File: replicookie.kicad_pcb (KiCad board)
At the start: 2 copper layers, 152.4 x 114.3 mm, 130 parts, among them J1001 Conn_02x03_Odd_Even, J1002 Conn_01x08_Female, J1003 Screw_Terminal_01x04, J1005 Conn_01x08_Female, J1101 Conn_02x03_Odd_Even, J1102 Conn_01x08_Female, J1103 Screw_Terminal_01x04, J1105 Conn_01x08_Female, J1201 Conn_02x03_Odd_Even, J1202 Conn_01x08_Female, J1203 Screw_Terminal_01x04, J1205 Conn_01x08_Female, J1301 Conn_02x03_Odd_Even, J1302 Conn_01x08_Female, J1303 Screw_Terminal_01x04, J1305 Conn_01x08_Female, J1401 Conn_02x03_Odd_Even, J1402 Conn_01x08_Female, J1403 Screw_Terminal_01x04, J1405 Conn_01x08_Female, J301 JK0654219, J401 USB_A, J402 USB_A, J701 Conn_02x03_Odd_Even, J702 Conn_01x08_Female, J703 Screw_Terminal_01x04, J705 Conn_01x08_Female, J801 Conn_02x03_Odd_Even, J802 Conn_01x08_Female, J803 Screw_Terminal_01x04, J805 Conn_01x08_Female, J901 Conn_02x03_Odd_Even, J902 Conn_01x08_Female, J903 Screw_Terminal_01x04, J905 Conn_01x08_Female, P2 TFM-115-01-F-D-A, P3 TFM-120-01-F-D-A, U201 DS1307ZN+, U301 MIC33050-4YHL, U302 KSZ9031RNXCA, U303 ASDMB-25.000MHz, U304 74LVC2G07, U305 TXS0102DCU, U401 ASDMB-24.000MHz-C, U402 ASDMB-26.000MHz-C, U403 USB3343, U404 74LVC1G07, U405 USB2514B_Bi, X201 ASE-xxxMHz

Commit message: Place motor drivers, start layout of Ethernet PHY
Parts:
- removed the C327 at (118.7, 9.74)
- added C312: 0.1U, Capacitor_SMD:C_0402_1005Metric, F.Cu at (156.8, 45.1)
- C201, C315, C401, C402, C403, C404, C405, C406, C408, C409: footprint Capacitor_SMD:C_0603_1608Metric -> Capacitor_SMD:C_0402_1005Metric
- C301: footprint Capacitor_SMD:C_0603_1608Metric -> Capacitor_SMD:C_0402_1005Metric; moved to B.Cu
- C302: renamed from C329; footprint Capacitor_SMD:C_0603_1608Metric -> Capacitor_SMD:C_0402_1005Metric
- C303: renamed from C302; footprint Capacitor_SMD:C_0603_1608Metric -> Capacitor_SMD:C_0402_1005Metric; moved to B.Cu
- C304: renamed from C330; footprint Capacitor_SMD:C_0603_1608Metric -> Capacitor_SMD:C_0402_1005Metric
- C310: renamed from C306; footprint Capacitor_SMD:C_0603_1608Metric -> Capacitor_SMD:C_0402_1005Metric
- C311: renamed from C309; footprint Capacitor_SMD:C_0603_1608Metric -> Capacitor_SMD:C_0402_1005Metric
- C313: renamed from C310; footprint Capacitor_SMD:C_0603_1608Metric -> Capacitor_SMD:C_0402_1005Metric
- C314: renamed from C311; footprint Capacitor_SMD:C_0603_1608Metric -> Capacitor_SMD:C_0402_1005Metric
- C316: renamed from C312; footprint Capacitor_SMD:C_0603_1608Metric -> Capacitor_SMD:C_0402_1005Metric
- C317: renamed from C316; footprint Capacitor_SMD:C_0603_1608Metric -> Capacitor_SMD:C_0402_1005Metric
- C318: renamed from C313; footprint Capacitor_SMD:C_0603_1608Metric -> Capacitor_SMD:C_0402_1005Metric
- C319: renamed from C314; footprint Capacitor_SMD:C_0603_1608Metric -> Capacitor_SMD:C_0402_1005Metric
- C320: renamed from C317; footprint Capacitor_SMD:C_0603_1608Metric -> Capacitor_SMD:C_0402_1005Metric
- C321: renamed from C318; footprint Capacitor_SMD:C_0603_1608Metric -> Capacitor_SMD:C_0402_1005Metric
- C322: renamed from C319; footprint Capacitor_SMD:C_0603_1608Metric -> Capacitor_SMD:C_0402_1005Metric
- C323: renamed from C321; footprint Capacitor_SMD:C_0603_1608Metric -> Capacitor_SMD:C_0402_1005Metric
- C324: renamed from C320; footprint Capacitor_SMD:C_0603_1608Metric -> Capacitor_SMD:C_0402_1005Metric
- C325: renamed from C322; footprint Capacitor_SMD:C_0603_1608Metric -> Capacitor_SMD:C_0402_1005Metric
- C327: renamed from C323; footprint Capacitor_SMD:C_0603_1608Metric -> Capacitor_SMD:C_0402_1005Metric
- C328: renamed from C324; footprint Capacitor_SMD:C_0603_1608Metric -> Capacitor_SMD:C_0402_1005Metric
- C329: renamed from C326; footprint Capacitor_SMD:C_0603_1608Metric -> Capacitor_SMD:C_0402_1005Metric
- C330: renamed from C328; footprint Capacitor_SMD:C_0603_1608Metric -> Capacitor_SMD:C_0402_1005Metric
- J1002: renamed from J1003; footprint TerminalBlock_Phoenix:TerminalBlock_Phoenix_PT-1,5-4-5.0-H_1x04_P5.00mm_Horizontal -> TerminalBlock_Phoenix:TerminalBlock_Phoenix_MPT-0,5-4-2.54_1x04_P2.54mm_Horizontal
- J1102: renamed from J1103; footprint TerminalBlock_Phoenix:TerminalBlock_Phoenix_PT-1,5-4-5.0-H_1x04_P5.00mm_Horizontal -> TerminalBlock_Phoenix:TerminalBlock_Phoenix_MPT-0,5-4-2.54_1x04_P2.54mm_Horizontal
- J1202: renamed from J1203; footprint TerminalBlock_Phoenix:TerminalBlock_Phoenix_PT-1,5-4-5.0-H_1x04_P5.00mm_Horizontal -> TerminalBlock_Phoenix:TerminalBlock_Phoenix_MPT-0,5-4-2.54_1x04_P2.54mm_Horizontal
- J1302: renamed from J1303; footprint TerminalBlock_Phoenix:TerminalBlock_Phoenix_PT-1,5-4-5.0-H_1x04_P5.00mm_Horizontal -> TerminalBlock_Phoenix:TerminalBlock_Phoenix_MPT-0,5-4-2.54_1x04_P2.54mm_Horizontal
- J1402: renamed from J1403; footprint TerminalBlock_Phoenix:TerminalBlock_Phoenix_PT-1,5-4-5.0-H_1x04_P5.00mm_Horizontal -> TerminalBlock_Phoenix:TerminalBlock_Phoenix_MPT-0,5-4-2.54_1x04_P2.54mm_Horizontal
- J702: renamed from J703; footprint TerminalBlock_Phoenix:TerminalBlock_Phoenix_PT-1,5-4-5.0-H_1x04_P5.00mm_Horizontal -> TerminalBlock_Phoenix:TerminalBlock_Phoenix_MPT-0,5-4-2.54_1x04_P2.54mm_Horizontal
- J802: renamed from J803; footprint TerminalBlock_Phoenix:TerminalBlock_Phoenix_PT-1,5-4-5.0-H_1x04_P5.00mm_Horizontal -> TerminalBlock_Phoenix:TerminalBlock_Phoenix_MPT-0,5-4-2.54_1x04_P2.54mm_Horizontal
- J902: renamed from J903; footprint TerminalBlock_Phoenix:TerminalBlock_Phoenix_PT-1,5-4-5.0-H_1x04_P5.00mm_Horizontal -> TerminalBlock_Phoenix:TerminalBlock_Phoenix_MPT-0,5-4-2.54_1x04_P2.54mm_Horizontal
- R1001, R1101, R1201, R1301, R1401, R701, R801, R901, U301: moved to B.Cu
- moved R1401 251.7 mm to (185.4, 134.6), turned to -90 degrees
- moved C1401 248.8 mm to (181.6, 133.3)
- moved R801 246.2 mm to (71.1, 134.6), turned to -90 degrees
- moved R701 246.1 mm to (52.1, 134.6), turned to -90 degrees
- moved R1001 245.6 mm to (109.2, 134.6), turned to -90 degrees
- moved C801 241.0 mm to (67.3, 133.3)
- moved C1001 240.7 mm to (105.4, 133.3)
- moved R1101 240.0 mm to (128.3, 134.6), turned to -90 degrees
- moved C1101 236.3 mm to (124.5, 133.3)
- moved R1201 235.2 mm to (147.3, 134.6), turned to -90 degrees
- moved R1301 232.1 mm to (166.4, 134.6), turned to -90 degrees
- moved C1201 231.0 mm to (143.5, 133.3)
- moved C1301 228.9 mm to (162.6, 133.3)
- moved R901 219.6 mm to (90.2, 134.6), turned to -90 degrees
- moved C901 215.2 mm to (86.4, 133.3)
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- renumbered C303 to C305, C304 to C306, C305 to C307, C307 to C308, C308 to C309, C325 to C326, J1002 to J1001, J1001 to J1003, J1005 to J1004, J1102 to J1101, J1101 to J1103, J1105 to J1104, J1202 to J1201, J1201 to J1203, J1205 to J1204, J1302 to J1301, J1301 to J1303, J1305 to J1304, J1402 to J1401, J1401 to J1403, J1405 to J1404, J702 to J701, J701 to J703, J705 to J704, J802 to J801, J801 to J803, J805 to J804, J902 to J901, J901 to J903, J905 to J904, P2 to P501, P3 to P502, PA1 to PA501, PA2 to PA502, PB1 to PB501, PB2 to PB502, PC1 to PC501, U305 to U302, U302 to U303, U303 to U304, U304 to U305
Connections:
- net /ZYNQ_I2C0.SCL renamed /SCL
- net /ZYNQ_I2C0.SDA renamed /SDA
- net Net-(C302-Pad2) renamed /Ethernet/CFF
- D302 pad 1: /~RESET -> /~RESET_1
- J1003 pad 5: GNDD -> GND
- J1003 pad 6: GNDD -> GND
- J1103 pad 5: GNDD -> GND
- J1103 pad 6: GNDD -> GND
- J1203 pad 5: GNDD -> GND
- J1203 pad 6: GNDD -> GND
- J1303 pad 5: GNDD -> GND
- J1303 pad 6: GNDD -> GND
- J1403 pad 5: GNDD -> GND
- J1403 pad 6: GNDD -> GND
- J703 pad 5: GNDD -> GND
- J703 pad 6: GNDD -> GND
- J803 pad 5: GNDD -> GND
- J803 pad 6: GNDD -> GND
- J903 pad 5: GNDD -> GND
- J903 pad 6: GNDD -> GND
- P501 pad 10: GNDD -> GND
- P501 pad 20: GNDD -> GND
- P501 pad 27: GNDD -> GND
- P501 pad 28: GNDD -> GND
- P501 pad 5: GNDD -> GND
- P501 pad 6: GNDD -> GND
- P501 pad 9: GNDD -> GND
- P502 pad 10: GNDD -> GND
- P502 pad 15: GNDD -> GND
- P502 pad 16: GNDD -> GND
- P502 pad 21: GNDD -> GND
- P502 pad 22: GNDD -> GND
- P502 pad 27: GNDD -> GND
- P502 pad 28: GNDD -> GND
- P502 pad 33: GNDD -> GND
- P502 pad 34: GNDD -> GND
- P502 pad 9: GNDD -> GND
- PA501 pad 10: GNDD -> GND
- PA501 pad 15: GNDD -> GND
- PA501 pad 16: GNDD -> GND
- PA501 pad 21: GNDD -> GND
- PA501 pad 22: GNDD -> GND
- PA501 pad 27: GNDD -> GND
- PA501 pad 28: GNDD -> GND
- PA501 pad 33: GNDD -> GND
- PA501 pad 34: GNDD -> GND
- PA501 pad 9: GNDD -> GND
- PA502 pad 10: GNDD -> GND
- PA502 pad 15: GNDD -> GND
- PA502 pad 16: GNDD -> GND
- PA502 pad 21: GNDD -> GND
- PA502 pad 22: GNDD -> GND
- PA502 pad 27: GNDD -> GND
- PA502 pad 28: GNDD -> GND
- PA502 pad 33: GNDD -> GND
- PA502 pad 34: GNDD -> GND
- PA502 pad 9: GNDD -> GND
- PB501 pad 10: GNDD -> GND
- PB501 pad 15: GNDD -> GND
- PB501 pad 16: GNDD -> GND
- PB501 pad 21: GNDD -> GND
- PB501 pad 22: GNDD -> GND
- PB501 pad 27: GNDD -> GND
- PB501 pad 28: GNDD -> GND
- PB501 pad 33: GNDD -> GND
- PB501 pad 34: GNDD -> GND
- PB501 pad 9: GNDD -> GND
- PB502 pad 10: GNDD -> GND
- PB502 pad 15: GNDD -> GND
- PB502 pad 16: GNDD -> GND
- PB502 pad 21: GNDD -> GND
- PB502 pad 22: GNDD -> GND
- PB502 pad 27: GNDD -> GND
- PB502 pad 28: GNDD -> GND
- PB502 pad 33: GNDD -> GND
- PB502 pad 34: GNDD -> GND
- PB502 pad 9: GNDD -> GND
- PC501 pad 10: GNDD -> GND
- PC501 pad 15: GNDD -> GND
- PC501 pad 16: GNDD -> GND
- PC501 pad 21: GNDD -> GND
- PC501 pad 22: GNDD -> GND
- PC501 pad 27: GNDD -> GND
- PC501 pad 28: GNDD -> GND
- PC501 pad 33: GNDD -> GND
- PC501 pad 34: GNDD -> GND
- PC501 pad 9: GNDD -> GND
- U302 pad 1: /Ethernet/MDIO -> /Ethernet/MDC
- U302 pad 4: /ETHERNET.MDIO -> /ETHERNET.MDC
- U302 pad 5: /ETHERNET.MDC -> /ETHERNET.MDIO
- U302 pad 8: /Ethernet/MDC -> /Ethernet/MDIO
- U403 pad 22: /~RESET_1 -> /~RESET
- U404 pad 2: /~RESET_1 -> /~RESET
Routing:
- added copper zone on In2.Cu, net +3V3
- added copper zone on F.Cu, net GND
- added copper zone on In1.Cu, net GND
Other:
- copper layers 2 -> 4

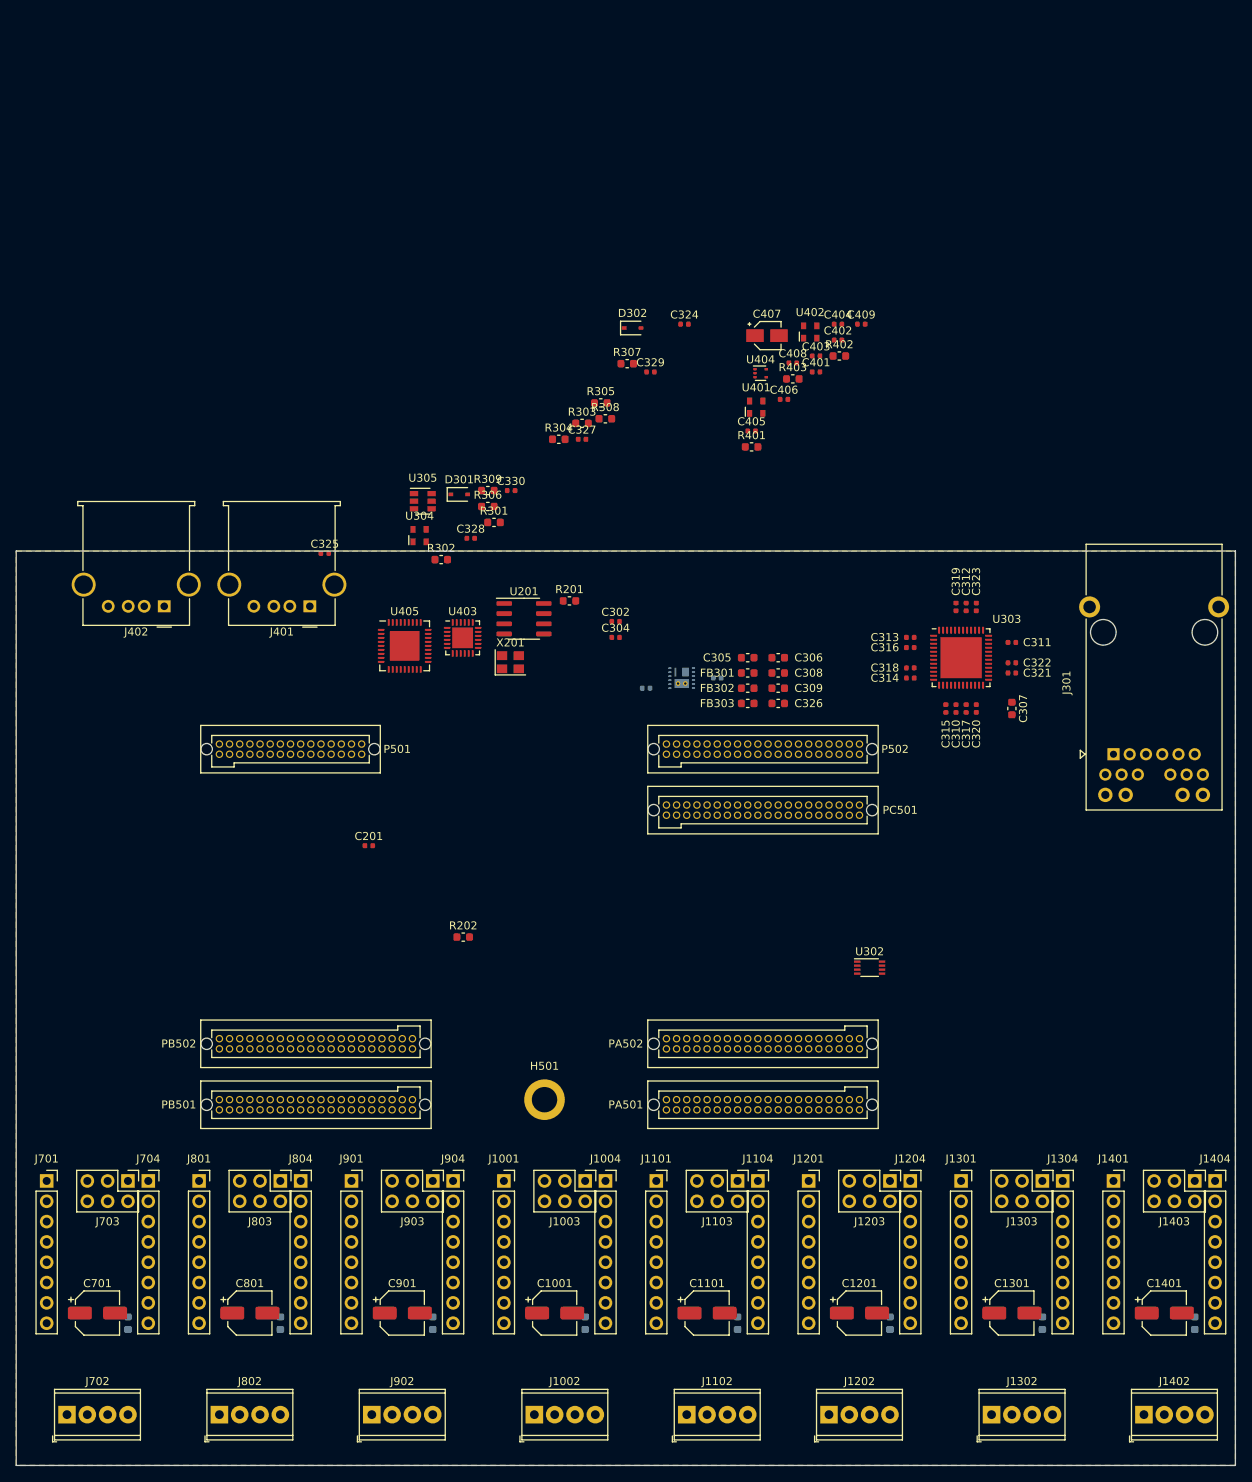
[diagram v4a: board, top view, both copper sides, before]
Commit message: Add FTDI chip
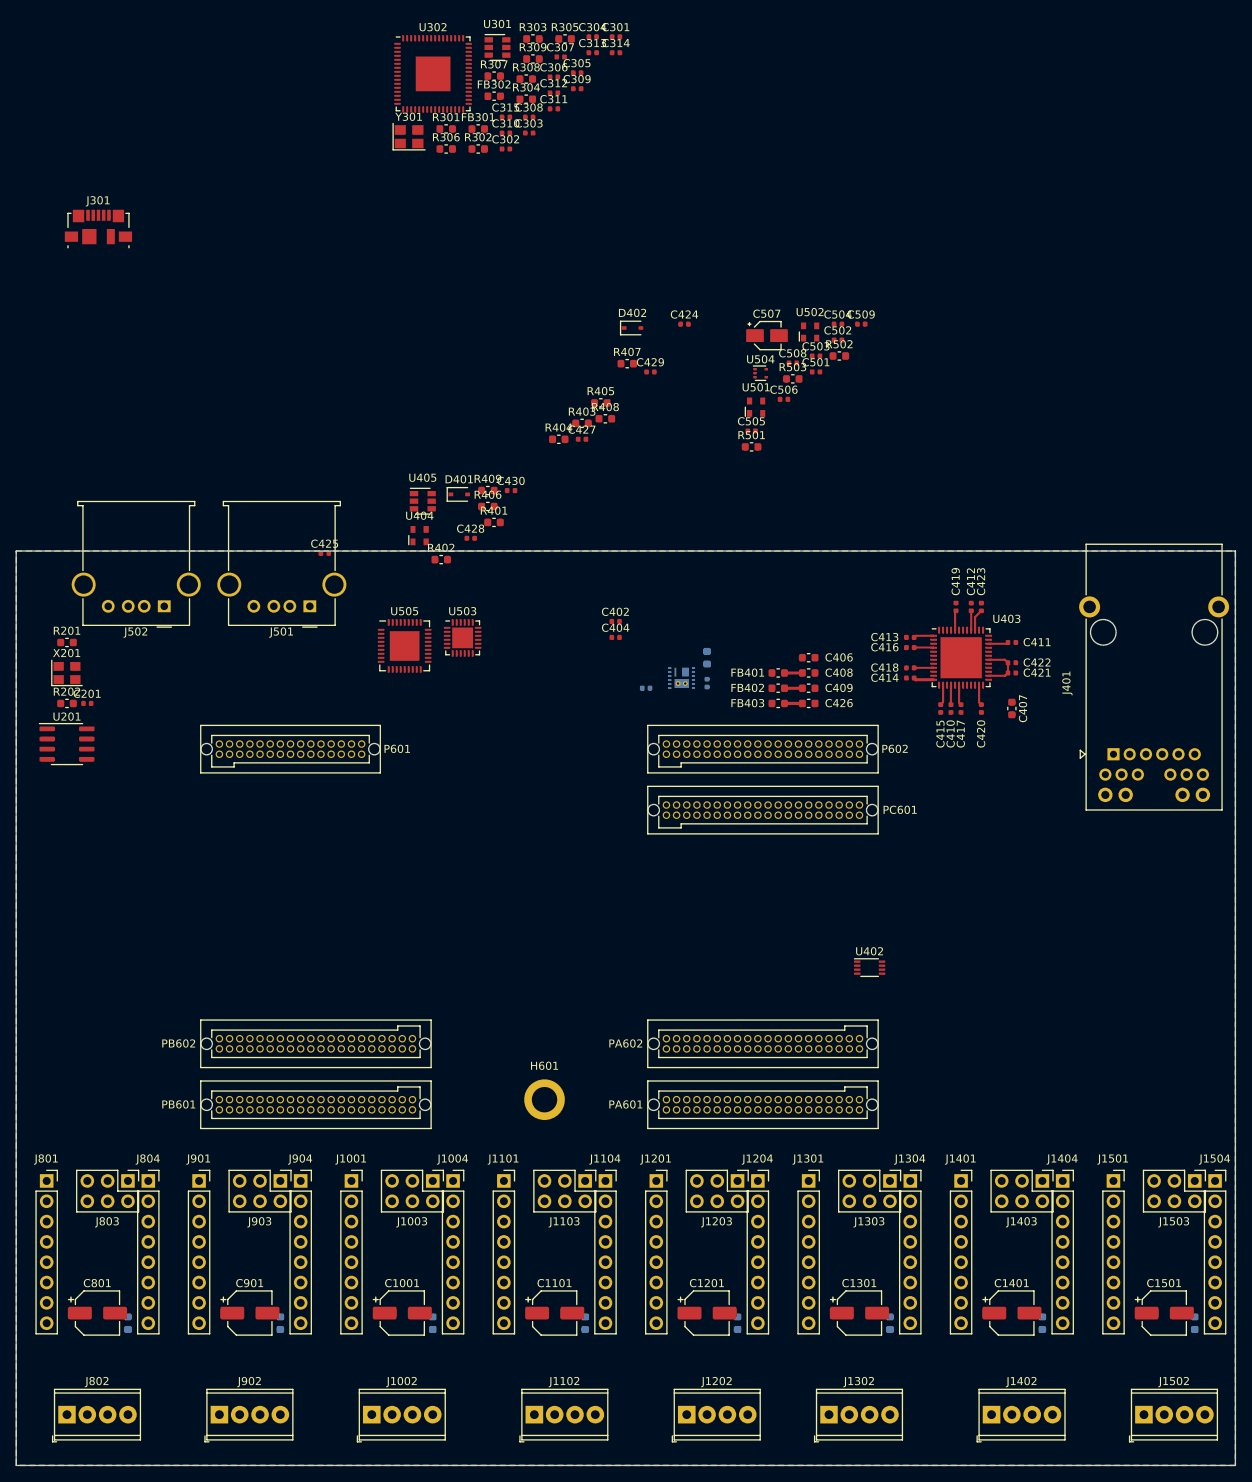
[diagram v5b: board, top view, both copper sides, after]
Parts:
- added C301: 27p, Capacitor_SMD:C_0402_1005Metric, F.Cu at (113.1, -26.2)
- added C302: 0.1u, Capacitor_SMD:C_0402_1005Metric, F.Cu at (99.3, -12.2)
- added C303: 27p, Capacitor_SMD:C_0402_1005Metric, F.Cu at (102.2, -14.1)
- added C304: 4.7u, Capacitor_SMD:C_0402_1005Metric, F.Cu at (110.2, -26.2)
- added C305: 4.7u, Capacitor_SMD:C_0402_1005Metric, F.Cu at (108.2, -21.7)
- added C306: 3.3u, Capacitor_SMD:C_0402_1005Metric, F.Cu at (105.3, -21.2)
- added C307: 0.1u, Capacitor_SMD:C_0402_1005Metric, F.Cu at (106.2, -23.7)
- added C308: 0.1u, Capacitor_SMD:C_0402_1005Metric, F.Cu at (102.2, -16.1)
- added C309: 0.1u, Capacitor_SMD:C_0402_1005Metric, F.Cu at (108.2, -19.7)
- added C310: 0.1u, Capacitor_SMD:C_0402_1005Metric, F.Cu at (99.3, -14.1)
- added C311: 0.1u, Capacitor_SMD:C_0402_1005Metric, F.Cu at (105.3, -17.2)
- added C312: 0.1u, Capacitor_SMD:C_0402_1005Metric, F.Cu at (105.3, -19.2)
- added C313: 0.1u, Capacitor_SMD:C_0402_1005Metric, F.Cu at (110.2, -24.2)
- added C314: 0.1u, Capacitor_SMD:C_0402_1005Metric, F.Cu at (113.1, -24.2)
- added C315: 0.1u, Capacitor_SMD:C_0402_1005Metric, F.Cu at (99.3, -16.1)
- added FB301: 80 ohm 100 MHz, Inductor_SMD:L_0603_1608Metric, F.Cu at (95.9, -14.7)
- added FB302: 80 ohm 100 MHz, Inductor_SMD:L_0603_1608Metric, F.Cu at (97.8, -18.8)
- added J301: USB_B_Micro, Connector_USB:USB_Micro-B_Molex_47346-0001, F.Cu at (48.4, -2.40)
- added R301: 10k, Resistor_SMD:R_0603_1608Metric, F.Cu at (91.8, -14.7)
- added R302: 10k, Resistor_SMD:R_0603_1608Metric, F.Cu at (95.9, -12.2)
- added R303: 2k, Resistor_SMD:R_0603_1608Metric, F.Cu at (102.7, -25.9)
- added R304: 10k, Resistor_SMD:R_0603_1608Metric, F.Cu at (101.9, -18.4)
- added R305: 12k, Resistor_SMD:R_0603_1608Metric, F.Cu at (106.7, -25.9)
- added R306: 1k, Resistor_SMD:R_0603_1608Metric, F.Cu at (91.8, -12.2)
- added R307: 470, Resistor_SMD:R_0603_1608Metric, F.Cu at (97.8, -21.3)
- added R308: 4.7k, Resistor_SMD:R_0603_1608Metric, F.Cu at (101.9, -20.9)
- added R309: 10k, Resistor_SMD:R_0603_1608Metric, F.Cu at (102.7, -23.4)
- added U301: 93LCxxBxxOT, Package_TO_SOT_SMD:SOT-23-6, F.Cu at (98.3, -24.8)
- added U302: FT2232HQ, Package_DFN_QFN:QFN-64-1EP_9x9mm_P0.5mm_EP4.35x4.35mm, F.Cu at (90.2, -21.5)
- added Y301: ABM8-12.000MHZ-20, Crystal:Crystal_SMD_Abracon_ABM8G-4Pin_3.2x2.5mm, F.Cu at (87.2, -13.7)
- C405: renamed from C305; moved to B.Cu
- moved R201 63.0 mm to (44.5, 49.5)
- moved U201 59.2 mm to (44.5, 62.2)
- moved R202 57.5 mm to (44.5, 57.1)
- moved X201 55.4 mm to (44.5, 53.3)
- moved C201 39.4 mm to (47.0, 57.1)
- moved C405 5.08 mm to (124.5, 51.4), turned to 90 degrees
- moved C406 3.81 mm to (137.2, 51.4)
- moved C408 3.81 mm to (137.2, 53.3)
- moved C409 3.81 mm to (137.2, 55.2)
- moved C426 3.81 mm to (137.2, 57.1)
- moved FB401 3.81 mm to (133.3, 53.3)
- moved FB402 3.81 mm to (133.3, 55.2)
- moved FB403 3.81 mm to (133.3, 57.1)
- moved C403 1.42 mm to (124.5, 54.6), turned to -90 degrees
- moved C415 0.64 mm to (153.7, 57.8)
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- renumbered C901 to C1001, C1001 to C1101, C1101 to C1201, C1201 to C1301, C1301 to C1401, C1401 to C1501, C301 to C401, C302 to C402, C303 to C403, C304 to C404, C306 to C406, C307 to C407, C308 to C408, C309 to C409, C310 to C410, C311 to C411, C312 to C412, C313 to C413, C314 to C414, C315 to C415, C316 to C416, C317 to C417, C318 to C418, C319 to C419, C320 to C420, C321 to C421, C322 to C422, C323 to C423, C324 to C424, C325 to C425, C326 to C426, C327 to C427, C328 to C428, C329 to C429, C330 to C430, C401 to C501, C402 to C502, C403 to C503, C404 to C504, C405 to C505, C406 to C506, C407 to C507, C408 to C508, C409 to C509, C701 to C801, C801 to C901, D301 to D401, D302 to D402, FB301 to FB401, FB302 to FB402, FB303 to FB403, H501 to H601, J901 to J1001, J902 to J1002, J903 to J1003, J904 to J1004, J1001 to J1101, J1002 to J1102, J1003 to J1103, J1004 to J1104, J1101 to J1201, J1102 to J1202, J1103 to J1203, J1104 to J1204, J1201 to J1301, J1202 to J1302, J1203 to J1303, J1204 to J1304, J1301 to J1401, J1302 to J1402, J1303 to J1403, J1304 to J1404, J1401 to J1501, J1402 to J1502, J1403 to J1503, J1404 to J1504, J301 to J401, J401 to J501, J402 to J502, J701 to J801, J702 to J802, J703 to J803, J704 to J804, J801 to J901, J802 to J902, J803 to J903, J804 to J904, P501 to P601, P502 to P602, PA501 to PA601, PA502 to PA602, PB501 to PB601, PB502 to PB602, PC501 to PC601, R901 to R1001, R1001 to R1101, R1101 to R1201, R1201 to R1301, R1301 to R1401, R1401 to R1501, R301 to R401, R302 to R402, R303 to R403, R304 to R404, R305 to R405, R306 to R406, R307 to R407, R308 to R408, R309 to R409, R401 to R501, R402 to R502, R403 to R503, R701 to R801, R801 to R901, U301 to U401, U302 to U402, U303 to U403, U304 to U404, U305 to U405, U401 to U501, U402 to U502, U403 to U503, U404 to U504, U405 to U505
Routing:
- net /Ethernet/DVDDL: track 0.00 -> 16.8 mm
- net +1V8: track 0.00 -> 7.36 mm
- net /Ethernet/AVDDH: track 0.00 -> 7.27 mm
- net /Ethernet/AVDDL: track 0.00 -> 7.11 mm
- net /Ethernet/AVDDL_PLL: track 0.00 -> 4.71 mm
- added copper zone on B.Cu, net GND
- removed copper zone on In2.Cu, net +3V3
